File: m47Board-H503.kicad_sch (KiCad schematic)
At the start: 42 parts, among them J1 USB_C_Receptacle_USB2.0_14P, J3 Conn_01x15_Pin, J4 Conn_01x10_Pin, J5 Conn_01x15_Pin, SW1 SW_Push, SW2 SW_Push, SW3 SW_Push, U1 AP2114H-3.3TRG1, U2 STM32H503CBTx, U3 USBLC6-2SC6, Y1 CX3225FB16000F0FZZH1 16MHz, Y2 ABS07-32.768KHZ-T

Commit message: Update PCB layout
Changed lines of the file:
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@@
 		(rev "0.1")
 		(company "m47eus2")
+		(comment 1 "https://github.com/m47eus2/m47Board-H503")
 	)

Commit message: Route some traces, do some silkscreen, change USB-C symbol, change larger caps footprints to 0603
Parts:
- removed J1: USB_C_Receptacle_USB2.0_14P, Connector_USB:USB_C_Receptacle_GCT_USB4105-xx-A_16P_TopMnt_Horizontal, symbol Connector:USB_C_Receptacle_USB2.0_14P
- added J1: USB_C_Receptacle_USB2.0_16P, Connector_USB:USB_C_Receptacle_GCT_USB4105-xx-A_16P_TopMnt_Horizontal, symbol Connector:USB_C_Receptacle_USB2.0_16P
- C12, C13, C7: footprint Capacitor_SMD:C_0805_2012Metric_Pad1.18x1.45mm_HandSolder -> Capacitor_SMD:C_0603_1608Metric_Pad1.08x0.95mm_HandSolder
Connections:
- net GND: now also J1.A1 (GND), J1.A12 (GND), J1.B1 (GND), J1.B12 (GND)
- net USB-C-CC1: now also J1.A5 (CC1)
- net USB-C-CC2: now also J1.B5 (CC2)
- net VBUS: now also J1.A4 (VBUS), J1.A9 (VBUS), J1.B4 (VBUS), J1.B9 (VBUS)
- net at U3.4 (I/O2): now also J1.A7 (D-), J1.B7 (D-)
- net at U3.6 (I/O1): now also J1.A6 (D+), J1.B6 (D+)

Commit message: Add copper zones
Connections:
- net GND: now also J1.SH (SHIELD)
- no-connect marks 1 -> 0

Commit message: Route traces
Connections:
- net GND: now also J3.2 (Pin_2); no longer J3.3 (Pin_3)
- net PA15: now also J3.6 (Pin_6)
- net PB3: now also J3.7 (Pin_7)
- net PB4: now also J3.8 (Pin_8)
- net PB5: now also J3.9 (Pin_9)
- net PB6: now also J3.10 (Pin_10)
- net PB7: now also J3.11 (Pin_11)
- net PB8: now also J3.12 (Pin_12)
- net PC13: now also J3.13 (Pin_13)
- net SWCLK: now also J3.4 (Pin_4); no longer J3.2 (Pin_2)
- net SWDIO: now also J3.3 (Pin_3); no longer J3.4 (Pin_4)
- net at R7.2: now also J3.15 (Pin_15)
- net at J3.14 (Pin_14): now also R6.2
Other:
- moved on the sheet: R6, R7

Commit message: Route tracks
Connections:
- net +3.3V: now also J3.15 (Pin_15), J5.1 (Pin_1)
- net GND: now also J3.14 (Pin_14), J5.14 (Pin_14), J5.2 (Pin_2)
- net PA0: now also J4.3 (Pin_3)
- net PA1: now also J4.4 (Pin_4)
- net PA10: now also J5.13 (Pin_13)
- net PA2: now also J4.5 (Pin_5)
- net PA3: now also J4.6 (Pin_6)
- net PA4: now also J4.7 (Pin_7)
- net PA5: now also J4.8 (Pin_8)
- net PA6: now also J4.9 (Pin_9)
- net PA7: now also J4.10 (Pin_10)
- net PA8: now also J5.11 (Pin_11)
- net PA9: now also J5.12 (Pin_12)
- net PB0: now also J5.3 (Pin_3)
- net PB1: now also J5.4 (Pin_4)
- net PB10: now also J5.6 (Pin_6)
- net PB12: now also J5.7 (Pin_7)
- net PB13: now also J5.8 (Pin_8)
- net PB14: now also J5.9 (Pin_9)
- net PB15: now also J5.10 (Pin_10)
- net PB2: now also J5.5 (Pin_5)
- net VBUS: now also J5.15 (Pin_15)
- net at R7.2: now also J4.2 (Pin_2); no longer J3.15 (Pin_15)
- net at J4.1 (Pin_1): now also R6.2
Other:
- moved on the sheet: J3, R6, R7

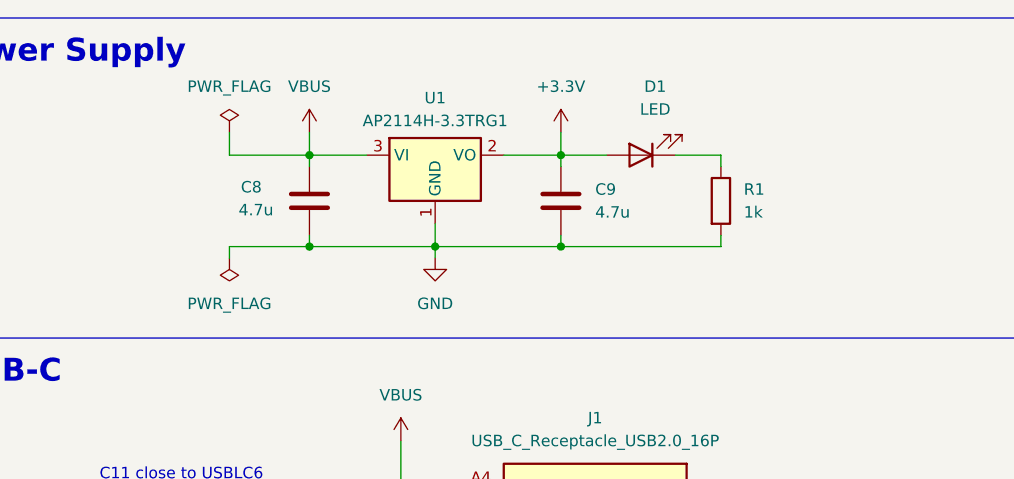
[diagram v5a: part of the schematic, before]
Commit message: Add VBUS LED, clean bottom copper
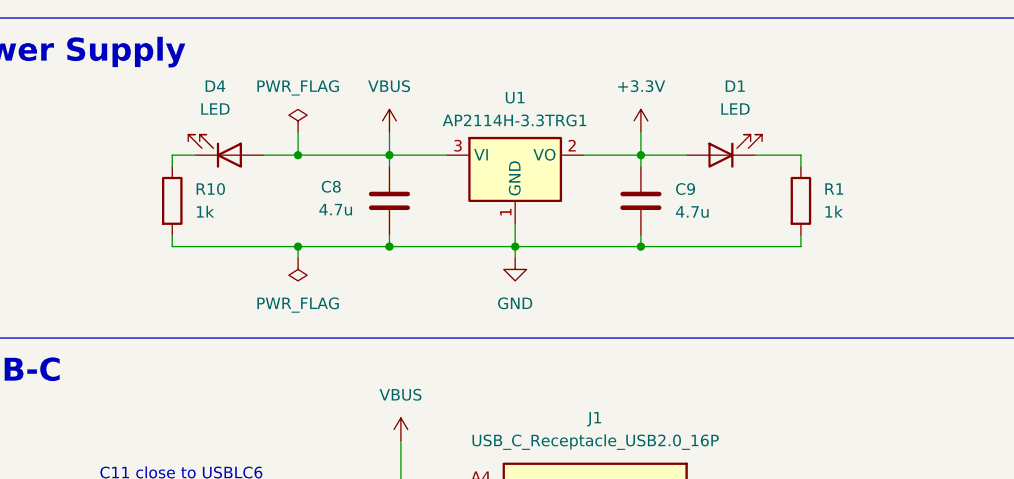
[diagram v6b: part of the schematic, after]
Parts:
- added D4: LED, LED_SMD:LED_0805_2012Metric_Pad1.15x1.40mm_HandSolder, symbol Device:LED
- added R10: 1k, Resistor_SMD:R_0402_1005Metric_Pad0.72x0.64mm_HandSolder, symbol Device:R
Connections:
- net GND: now also R10.2
- net VBUS: now also D4.2 (A)
- new net: D4.1 (K), R10.1
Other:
- moved on the sheet: C8, C9, D1, R1, U1

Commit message: Swap LDO, clean DRC
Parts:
- U1: value AP2114H-3.3TRG1 -> AP2114HA-3.3TRG1
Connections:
- net +3.3V: now also C8.1, U1.3 (VO); no longer C9.1, U1.2 (VO)
- net GND: now also U1.2 (GND); no longer U1.1 (GND)
- net VBUS: now also C9.1, U1.1 (VI); no longer C8.1, U1.3 (VI)
- no-connect marks 0 -> 2
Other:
- moved on the sheet: C8, C9
